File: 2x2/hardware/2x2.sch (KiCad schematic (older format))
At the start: 24 parts

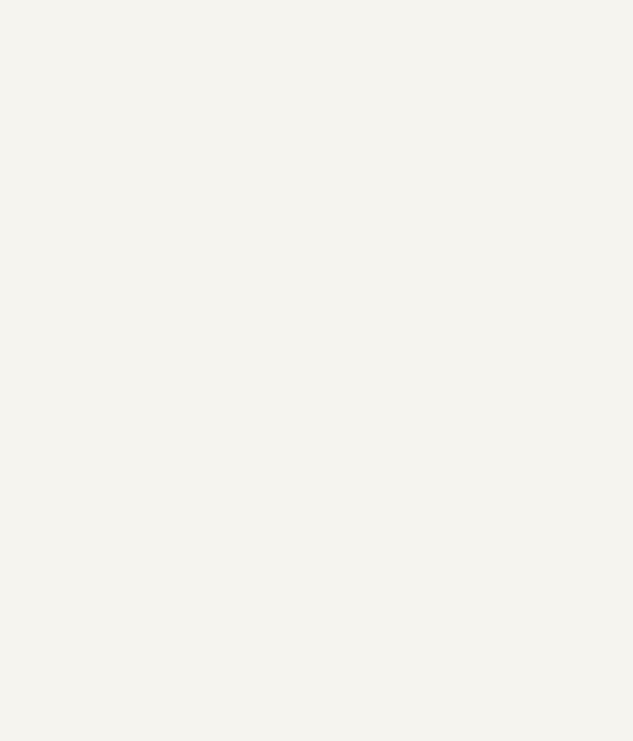
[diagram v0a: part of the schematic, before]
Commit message: Add switch and diodes matrix
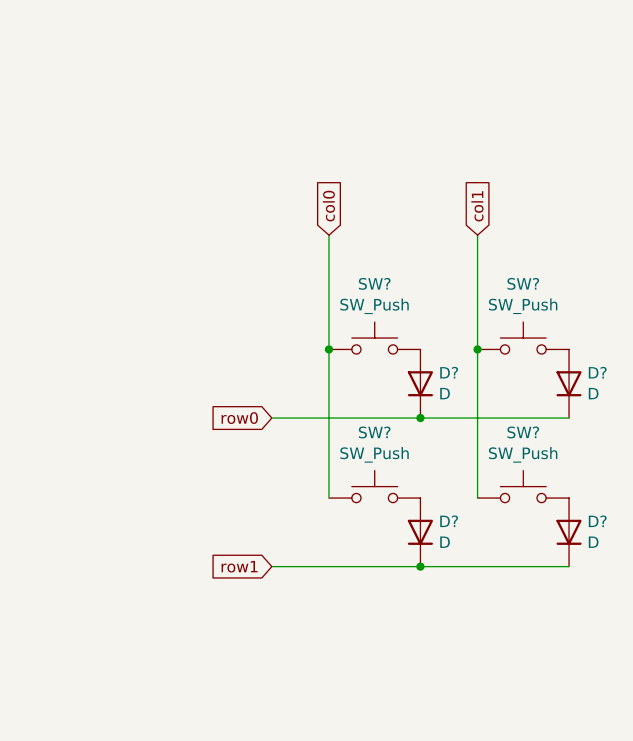
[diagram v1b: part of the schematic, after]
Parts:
- added D? (x4): D, symbol Device:D
- added SW? (x4): SW_Push, Button_Switch_Keyboard:SW_Cherry_MX_1.00u_PCB, symbol Switch:SW_Push
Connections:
- new net: D?.2 (A), SW?.2 (x4)
- new net col0: SW?.1, SW?.1
- new net col1: SW?.1, SW?.1
- new net row0: D?.1 (K), D?.1 (K)
- new net row1: D?.1 (K), D?.1 (K)
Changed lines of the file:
@@
 encoding utf-8
 Sheet 1 1
-Title ""
-Date ""
+Title "2x2"
+Date "2020-01-18"
 Rev ""
 Comp ""
@@
 Comment2 ""
 Comment3 ""
-Comment4 ""
+Comment4 "4 key keyboard"
 $EndDescr
 $Comp
@@
 	1    0    0    -1
 $EndComp
+$Comp
+L Switch:SW_Push SW?
+U 1 1 5E23CB9E
+P 10200 2500
+F 0 "SW?" H 10200 2785 50  0000 C CNN
+F 1 "SW_Push" H 10200 2694 50  0000 C CNN
+F 2 "Button_Switch_Keyboard:SW_Cherry_MX_1.00u_PCB" H 10200 2700 50  0001 C CNN
+F 3 "~" H 10200 2700 50  0001 C CNN
+	1    10200 2500
+	1    0    0    -1
+$EndComp
+Text GLabel 9750 2800 0    50   Input ~ 0
+row0
+Text GLabel 9750 3450 0    50   Input ~ 0
+row1
+Text GLabel 10000 2000 1    50   Input ~ 0
+col0
+Text GLabel 10650 2000 1    50   Input ~ 0
+col1
+$Comp
+L Device:D D?
+U 1 1 5E23FADA
+P 10400 2650
+F 0 "D?" V 10446 2570 50  0000 R CNN
+F 1 "D" V 10355 2570 50  0000 R CNN
+F 2 "" H 10400 2650 50  0001 C CNN
+F 3 "~" H 10400 2650 50  0001 C CNN
+	1    10400 2650
+	0    -1   -1   0
+$EndComp
+$Comp
+L Switch:SW_Push SW?
+U 1 1 5E24A1E2
+P 10850 2500
+F 0 "SW?" H 10850 2785 50  0000 C CNN
+F 1 "SW_Push" H 10850 2694 50  0000 C CNN
+F 2 "Button_Switch_Keyboard:SW_Cherry_MX_1.00u_PCB" H 10850 2700 50  0001 C CNN
+F 3 "~" H 10850 2700 50  0001 C CNN
+	1    10850 2500
+	1    0    0    -1
+$EndComp
+$Comp
+L Device:D D?
+U 1 1 5E24A1EC
+P 11050 2650
+F 0 "D?" V 11096 2570 50  0000 R CNN
+F 1 "D" V 11005 2570 50  0000 R CNN
+F 2 "" H 11050 2650 50  0001 C CNN
+F 3 "~" H 11050 2650 50  0001 C CNN
+	1    11050 2650
+	0    -1   -1   0
+$EndComp
+$Comp
+L Switch:SW_Push SW?
+U 1 1 5E262559
+P 10200 3150
+F 0 "SW?" H 10200 3435 50  0000 C CNN
+F 1 "SW_Push" H 10200 3344 50  0000 C CNN
+F 2 "Button_Switch_Keyboard:SW_Cherry_MX_1.00u_PCB" H 10200 3350 50  0001 C CNN
+F 3 "~" H 10200 3350 50  0001 C CNN
+	1    10200 3150
+	1    0    0    -1
+$EndComp
+$Comp
+L Device:D D?
+U 1 1 5E262563
+P 10400 3300
+F 0 "D?" V 10446 3220 50  0000 R CNN
+F 1 "D" V 10355 3220 50  0000 R CNN
+F 2 "" H 10400 3300 50  0001 C CNN
+F 3 "~" H 10400 3300 50  0001 C CNN
+	1    10400 3300
+	0    -1   -1   0
+$EndComp
+$Comp
+L Switch:SW_Push SW?
+U 1 1 5E2659FE
+P 10850 3150
+F 0 "SW?" H 10850 3435 50  0000 C CNN
+F 1 "SW_Push" H 10850 3344 50  0000 C CNN
+F 2 "Button_Switch_Keyboard:SW_Cherry_MX_1.00u_PCB" H 10850 3350 50  0001 C CNN
+F 3 "~" H 10850 3350 50  0001 C CNN
+	1    10850 3150
+	1    0    0    -1
+$EndComp
+$Comp
+L Device:D D?
+U 1 1 5E265A08
+P 11050 3300
+F 0 "D?" V 11096 3220 50  0000 R CNN
+F 1 "D" V 11005 3220 50  0000 R CNN
+F 2 "" H 11050 3300 50  0001 C CNN
+F 3 "~" H 11050 3300 50  0001 C CNN
+	1    11050 3300
+	0    -1   -1   0
+$EndComp
+Wire Wire Line
+	10000 2000 10000 2500
+Wire Wire Line
+	10000 3150 10000 2500
+Connection ~ 10000 2500
+Wire Wire Line
+	9750 2800 10400 2800
+Wire Wire Line
+	10650 2000 10650 2500
+Wire Wire Line
+	10650 2500 10650 3150
+Connection ~ 10650 2500
+Wire Wire Line
+	11050 2800 10400 2800
+Connection ~ 10400 2800
+Wire Wire Line
+	11050 3450 10400 3450
+Wire Wire Line
+	10400 3450 9750 3450
+Connection ~ 10400 3450
 $EndSCHEMATC

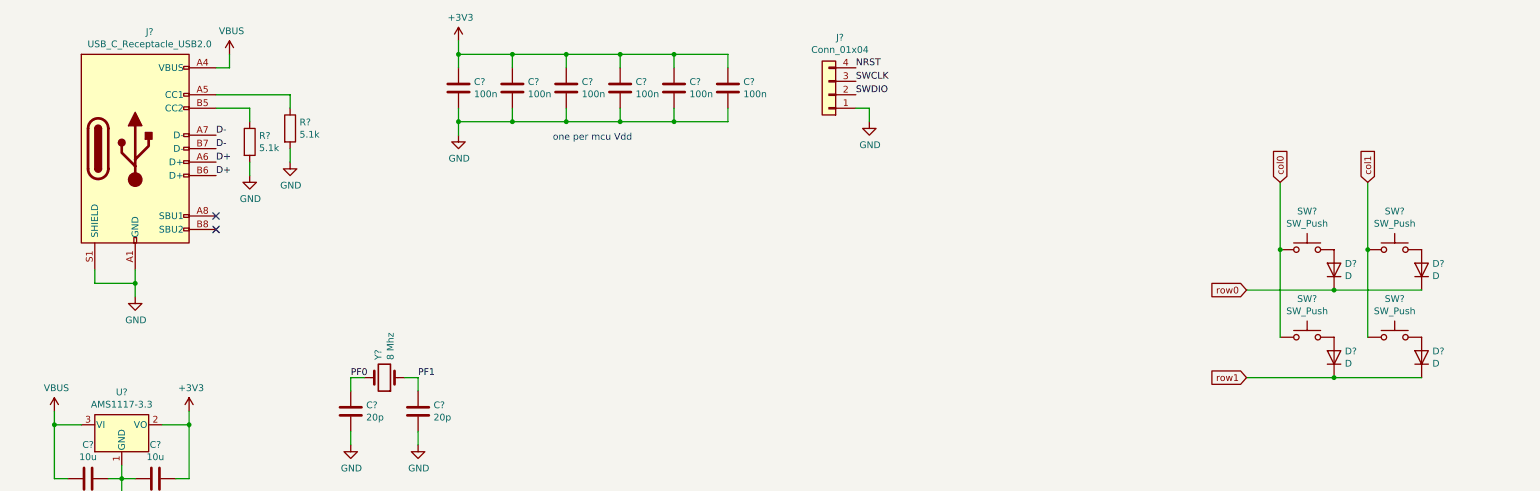
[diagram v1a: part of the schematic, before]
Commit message: Added a symbol for a switch, diode and led and wired matrix
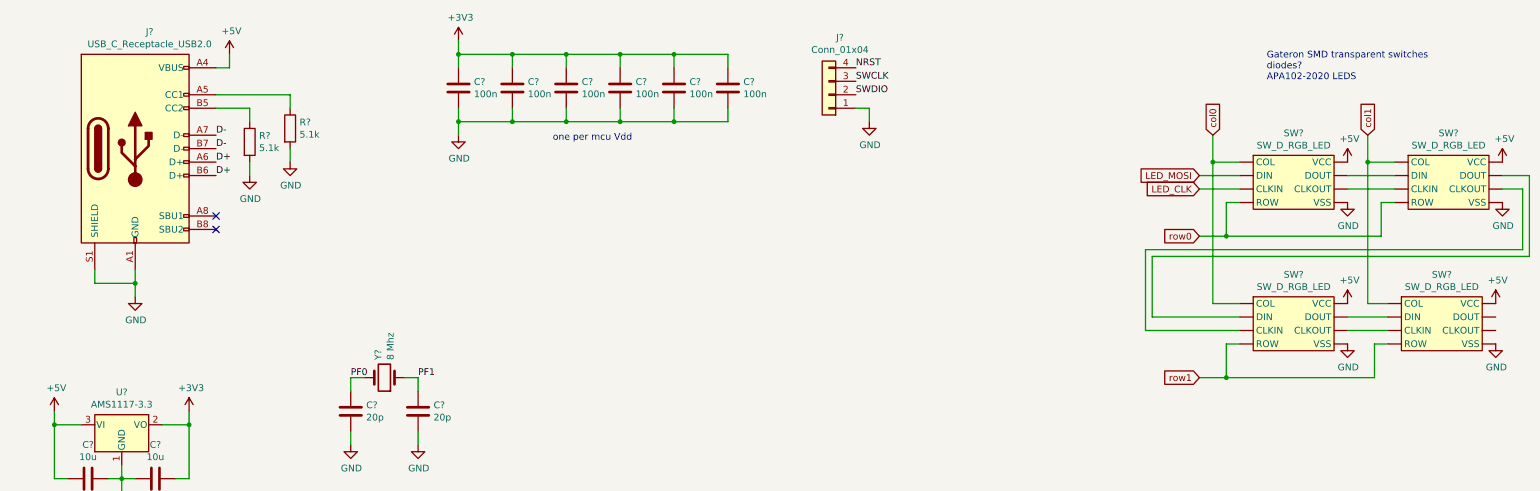
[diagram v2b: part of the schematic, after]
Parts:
- removed D? (x4): D, symbol Device:D
- removed SW? (x4): SW_Push, Button_Switch_Keyboard:SW_Cherry_MX_1.00u_PCB, symbol Switch:SW_Push
- added SW? (x4): SW_D_RGB_LED, symbol User_Modules:SW_D_RGB_LED
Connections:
- net GND: now also SW?.~ (VSS), SW?.~ (VSS), SW?.~ (VSS), SW?.~ (VSS)
- net col0: now also SW?.~ (VSS), SW?.~ (VSS)
- net col1: now also SW?.~ (VSS), SW?.~ (VSS)
- net row0: now also SW?.~ (VSS), SW?.~ (VSS)
- net row1: now also SW?.~ (VSS), SW?.~ (VSS)
- net VBUS renamed +5V
- net +5V: now also SW?.~ (VSS), SW?.~ (VSS), SW?.~ (VSS), SW?.~ (VSS)
- new net: SW?.~ (VSS), SW?.~ (VSS) (x6)
- new net LED_CLK: SW?.~ (VSS)
- new net LED_MOSI: SW?.~ (VSS)
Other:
- note added: "Gateron SMD transparent switches\ndiodes?\nAPA102-2020 LEDS"

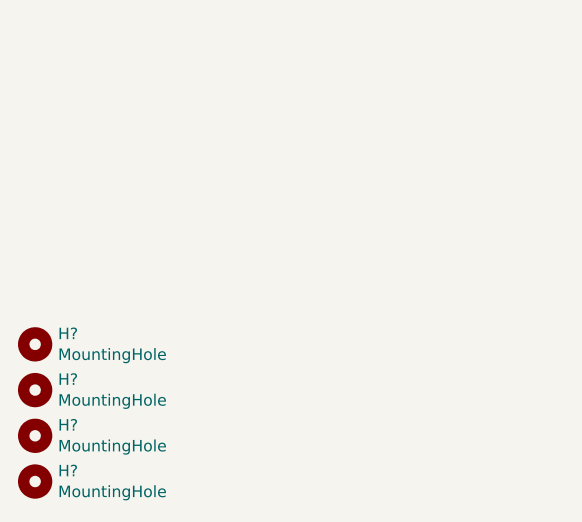
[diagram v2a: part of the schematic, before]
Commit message: Connect mounting holes to ground
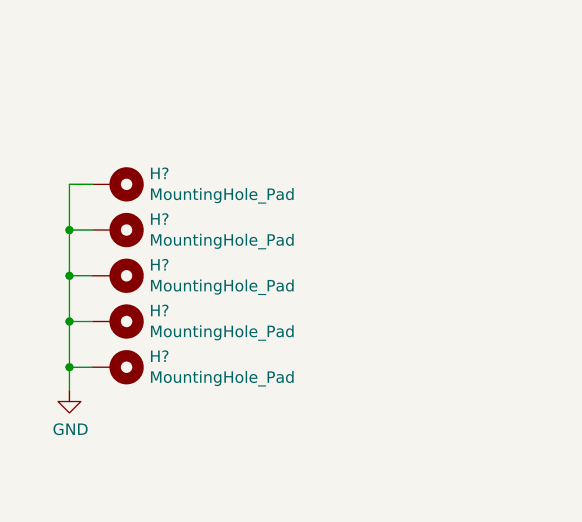
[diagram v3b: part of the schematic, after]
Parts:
- removed H? (x4): MountingHole, symbol Mechanical:MountingHole
- added H? (x5): MountingHole_Pad, symbol Mechanical:MountingHole_Pad
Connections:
- net GND: now also H?.1, H?.1, H?.1, H?.1, H?.1
- new net: SW?.~ (VSS), SW?.~ (VSS) (x6)
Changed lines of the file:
@@
 Wire Wire Line
 	900  3800 900  3700
-$Comp
-L Mechanical:MountingHole H?
-U 1 1 5E2A13A4
-P 650 10400
-F 0 "H?" H 750 10446 50  0000 L CNN
-F 1 "MountingHole" H 750 10355 50  0000 L CNN
-F 2 "" H 650 10400 50  0001 C CNN
-F 3 "~" H 650 10400 50  0001 C CNN
-	1    650  10400
-	1    0    0    -1
-$EndComp
-$Comp
-L Mechanical:MountingHole H?
-U 1 1 5E2A26D8
-P 650 10600
-F 0 "H?" H 750 10646 50  0000 L CNN
-F 1 "MountingHole" H 750 10555 50  0000 L CNN
-F 2 "" H 650 10600 50  0001 C CNN
-F 3 "~" H 650 10600 50  0001 C CNN
-	1    650  10600
-	1    0    0    -1
-$EndComp
-$Comp
-L Mechanical:MountingHole H?
-U 1 1 5E2A2954
-P 650 10800
-F 0 "H?" H 750 10846 50  0000 L CNN
-F 1 "MountingHole" H 750 10755 50  0000 L CNN
-F 2 "" H 650 10800 50  0001 C CNN
-F 3 "~" H 650 10800 50  0001 C CNN
-	1    650  10800
-	1    0    0    -1
-$EndComp
-$Comp
-L Mechanical:MountingHole H?
-U 1 1 5E2A2B41
-P 650 11000
-F 0 "H?" H 750 11046 50  0000 L CNN
-F 1 "MountingHole" H 750 10955 50  0000 L CNN
-F 2 "" H 650 11000 50  0001 C CNN
-F 3 "~" H 650 11000 50  0001 C CNN
-	1    650  11000
-	1    0    0    -1
-$EndComp
 Text GLabel 10650 1650 1    50   Input ~ 0
 col1
@@
 	9600 3450 10700 3450
 Connection ~ 9600 3450
+$Comp
+L Mechanical:MountingHole_Pad H?
+U 1 1 5E43DBA7
+P 1000 9700
+F 0 "H?" V 954 9850 50  0000 L CNN
+F 1 "MountingHole_Pad" V 1045 9850 50  0000 L CNN
+F 2 "" H 1000 9700 50  0001 C CNN
+F 3 "~" H 1000 9700 50  0001 C CNN
+	1    1000 9700
+	0    1    1    0
+$EndComp
+$Comp
+L Mechanical:MountingHole_Pad H?
+U 1 1 5E43EDA0
+P 1000 9900
+F 0 "H?" V 954 10050 50  0000 L CNN
+F 1 "MountingHole_Pad" V 1045 10050 50  0000 L CNN
+F 2 "" H 1000 9900 50  0001 C CNN
+F 3 "~" H 1000 9900 50  0001 C CNN
+	1    1000 9900
+	0    1    1    0
+$EndComp
+$Comp
+L Mechanical:MountingHole_Pad H?
+U 1 1 5E43EFBD
+P 1000 10100
+F 0 "H?" V 954 10250 50  0000 L CNN
+F 1 "MountingHole_Pad" V 1045 10250 50  0000 L CNN
+F 2 "" H 1000 10100 50  0001 C CNN
+F 3 "~" H 1000 10100 50  0001 C CNN
+	1    1000 10100
+	0    1    1    0
+$EndComp
+$Comp
+L Mechanical:MountingHole_Pad H?
+U 1 1 5E43F1D9
+P 1000 10300
+F 0 "H?" V 954 10450 50  0000 L CNN
+F 1 "MountingHole_Pad" V 1045 10450 50  0000 L CNN
+F 2 "" H 1000 10300 50  0001 C CNN
+F 3 "~" H 1000 10300 50  0001 C CNN
+	1    1000 10300
+	0    1    1    0
+$EndComp
+$Comp
+L Mechanical:MountingHole_Pad H?
+U 1 1 5E43F428
+P 1000 10500
+F 0 "H?" V 954 10650 50  0000 L CNN
+F 1 "MountingHole_Pad" V 1045 10650 50  0000 L CNN
+F 2 "" H 1000 10500 50  0001 C CNN
+F 3 "~" H 1000 10500 50  0001 C CNN
+	1    1000 10500
+	0    1    1    0
+$EndComp
+$Comp
+L power:GND #PWR?
+U 1 1 5E43F76F
+P 800 10600
+F 0 "#PWR?" H 800 10350 50  0001 C CNN
+F 1 "GND" H 805 10427 50  0000 C CNN
+F 2 "" H 800 10600 50  0001 C CNN
+F 3 "" H 800 10600 50  0001 C CNN
+	1    800  10600
+	1    0    0    -1
+$EndComp
+Wire Wire Line
+	800  10600 800  10500
+Wire Wire Line
+	800  9700 900  9700
+Wire Wire Line
+	900  9900 800  9900
+Connection ~ 800  9900
+Wire Wire Line
+	800  9900 800  9700
+Wire Wire Line
+	900  10100 800  10100
+Connection ~ 800  10100
+Wire Wire Line
+	800  10100 800  9900
+Wire Wire Line
+	900  10300 800  10300
+Connection ~ 800  10300
+Wire Wire Line
+	800  10300 800  10100
+Wire Wire Line
+	900  10500 800  10500
+Connection ~ 800  10500
+Wire Wire Line
+	800  10500 800  10300
 $EndSCHEMATC

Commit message: Add LED choice and add some footprints
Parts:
- C1, C10, C2, C5, C6, C7, C8, C9: renamed from C?; footprint (none) -> Capacitor_SMD:C_0805_2012Metric_Pad1.15x1.40mm_HandSolder
- C3, C4: renamed from C?; value 20p -> 22p; footprint (none) -> Capacitor_SMD:C_0805_2012Metric_Pad1.15x1.40mm_HandSolder
- H1, H2, H3, H4, H5: renamed from H?; footprint (none) -> MountingHole:MountingHole_3.2mm_M3_Pad
- J1: renamed from J?; footprint (none) -> Connector_USB:USB_C_Receptacle_XKB_U262-16XN-4BVC11
- J2: renamed from J?; value Conn_01x04 -> Programming connector
- gave numbers to parts that had none: 12
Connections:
- net LED_CLK: now also U2.21 (PA5)
- net LED_MOSI: now also U2.23 (PA7)
- net col0: now also U2.30 (PB11)
- net col1: now also U2.29 (PB10)
- net row0: now also U2.62 (PB9)
- net row1: now also U2.61 (PB8)
- new net: SW1.~ (VSS), SW4.~ (VSS) (x2)
- new net: SW2.~ (VSS), SW4.~ (VSS) (x2)
- new net: SW2.~ (VSS), SW3.~ (VSS) (x2)
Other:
- moved on the sheet: R2, R3
